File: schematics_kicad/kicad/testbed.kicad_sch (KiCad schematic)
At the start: 0 parts

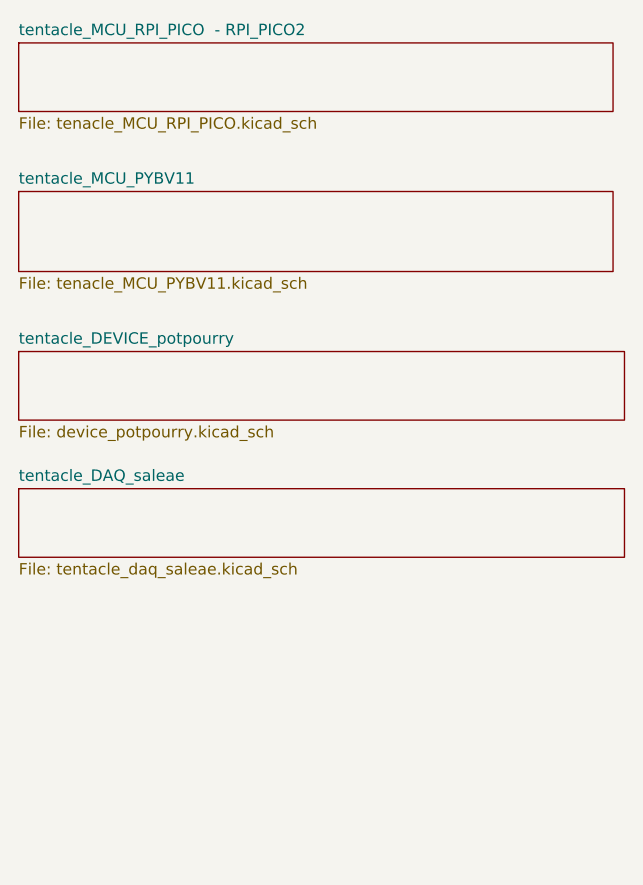
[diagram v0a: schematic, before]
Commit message: Lolin_D1/C3: wireint to allow use of DAQ. Kicad Schematics updated
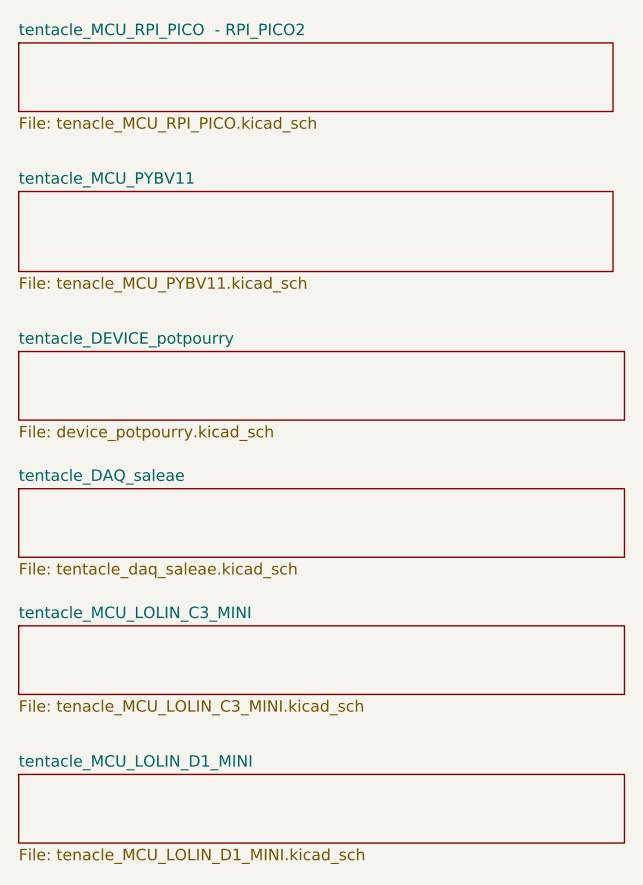
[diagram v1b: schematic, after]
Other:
- added sheet tentacle_MCU_LOLIN_C3_MINI (tenacle_MCU_LOLIN_C3_MINI.kicad_sch)
- added sheet tentacle_MCU_LOLIN_D1_MINI (tenacle_MCU_LOLIN_D1_MINI.kicad_sch)
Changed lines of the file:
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@@
+	)
+	(sheet
+		(at 36.83 114.3)
+		(size 67.31 7.62)
+		(fields_autoplaced yes)
+		(stroke
+			(width 0.1524)
+			(type solid)
+		)
+		(fill
+			(color 0 0 0 0.0000)
+		)
+		(property "Sheetname" "tentacle_MCU_LOLIN_D1_MINI"
+			(at 36.83 113.5884 0)
+			(effects
+				(font
+					(size 1.27 1.27)
+				)
+				(justify left bottom)
+			)
+		)
+		(property "Sheetfile" "tenacle_MCU_LOLIN_D1_MINI.kicad_sch"
+			(at 36.83 122.5046 0)
+			(effects
+				(font
+					(size 1.27 1.27)
+				)
+				(justify left top)
+			)
+		)
+		(instances
+			(project "testbed"
+				(path "/188054c4-74b7-429a-b3f5-c6f3151e27de"
+					(page "15")
+				)
+			)
+		)
 	)
 	(sheet
@@
 				)
 			)
+		)
+	)
+	(sheet
+		(at 36.83 97.79)
+		(size 67.31 7.62)
+		(fields_autoplaced yes)
+		(stroke
+			(width 0.1524)
+			(type solid)
+		)
+		(fill
+			(color 0 0 0 0.0000)
+		)
+		(property "Sheetname" "tentacle_MCU_LOLIN_C3_MINI"
+			(at 36.83 97.0784 0)
+			(effects
+				(font
+					(size 1.27 1.27)
+				)
+				(justify left bottom)
+			)
+		)
+		(property "Sheetfile" "tenacle_MCU_LOLIN_C3_MINI.kicad_sch"
+			(at 36.83 105.9946 0)
+			(effects
+				(font
+					(size 1.27 1.27)
+				)
+				(justify left top)
+			)
+		)
+		(instances
+			(project "testbed"
+				(path "/188054c4-74b7-429a-b3f5-c6f3151e27de"
+					(page "14")
+				)
+			)
